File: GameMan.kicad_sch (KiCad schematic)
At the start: 40 parts, among them J1 USB_C_Receptacle_USB2.0_16P, Q1 S8050, SW1 TS-1187A-B-A-B, SW10 TS-1187A-B-A-B, SW11 TS-1187A-B-A-B, SW12 TS-1187A-B-A-B, SW13 TS-1187A-B-A-B, SW2 TS-1187A-B-A-B, SW4 SW_SPST, SW5 TS-1187A-B-A-B, SW6 TS-1187A-B-A-B, SW7 TS-1187A-B-A-B, SW8 TS-1187A-B-A-B, SW9 TS-1187A-B-A-B, U1 ESP32-S3-DEVKITC-1-N8R2, U2 TP4056-42-ESOP8, U3 AMS1117-3.3

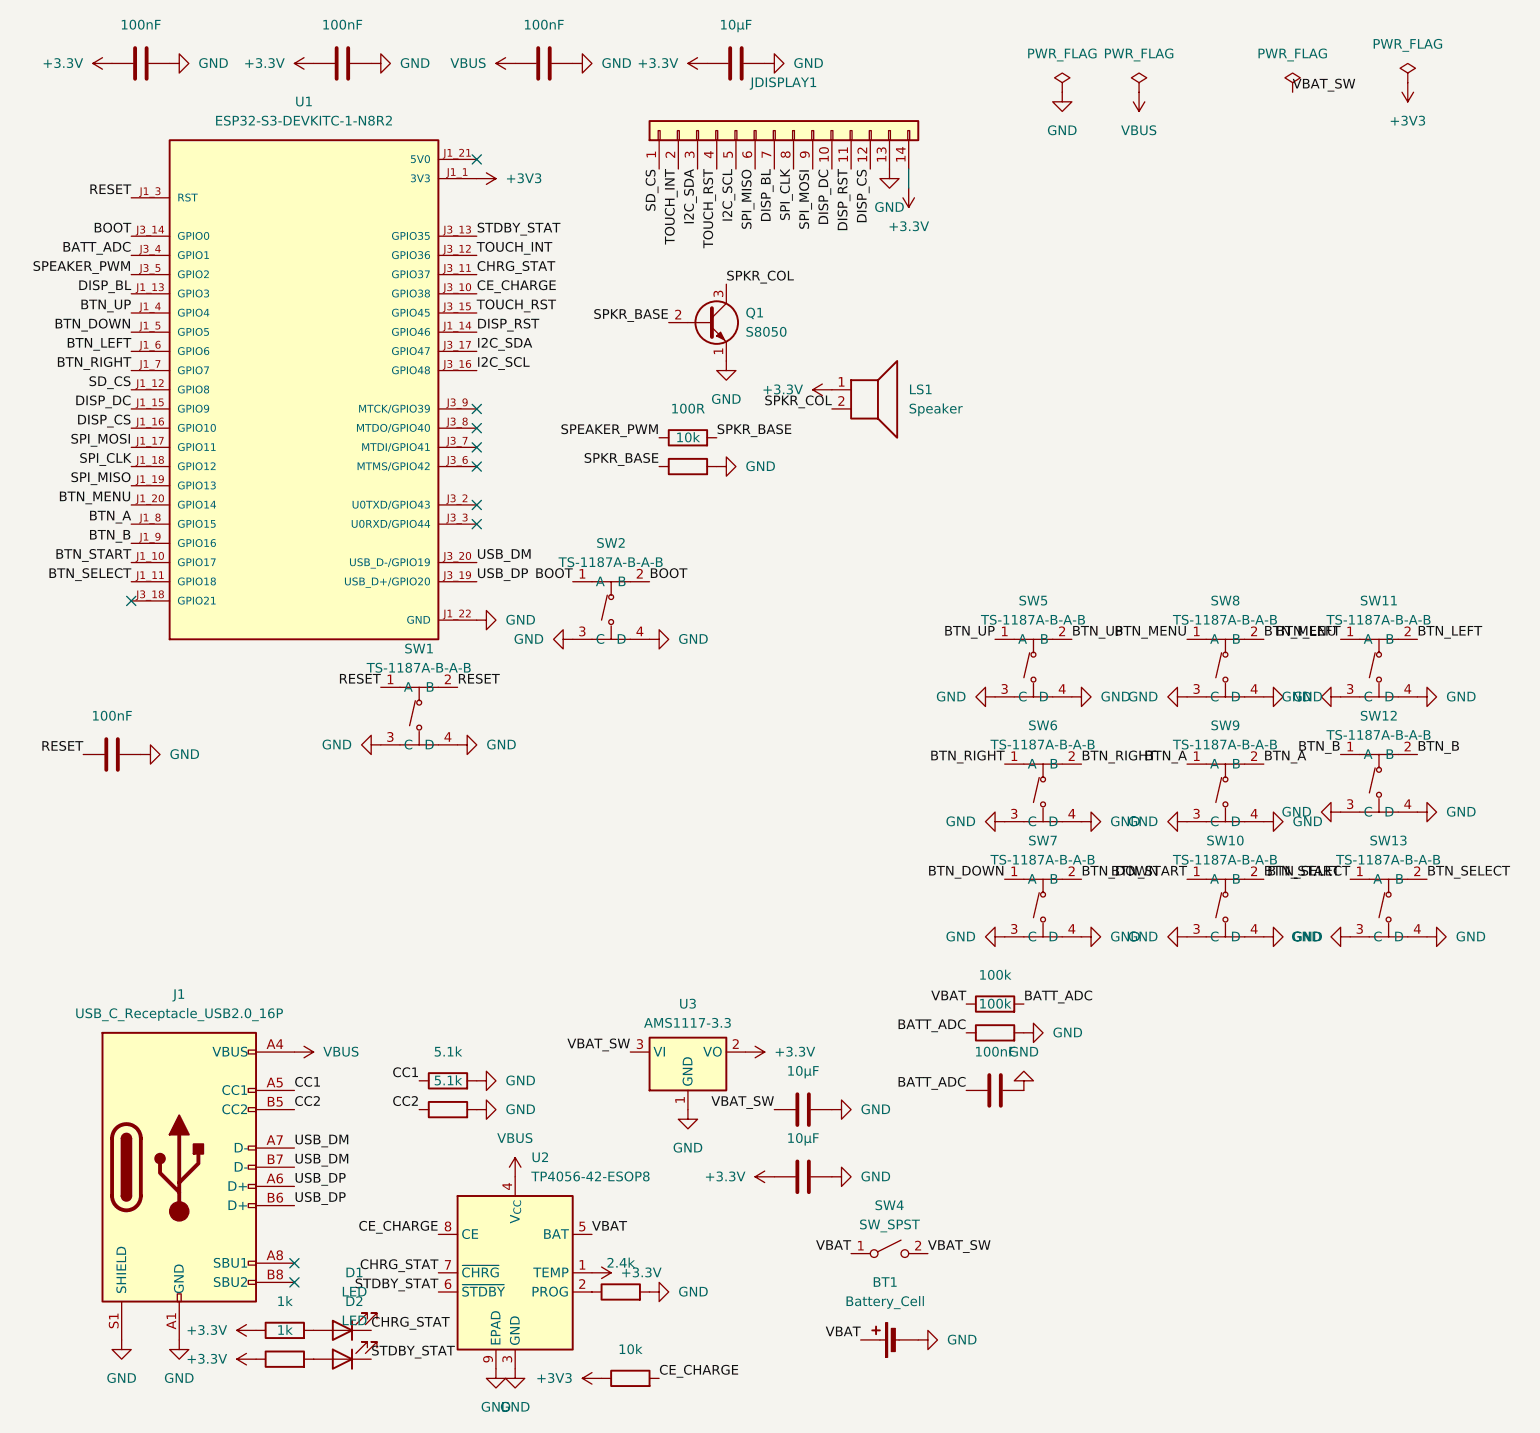
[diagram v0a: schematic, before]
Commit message: PCB layout complete
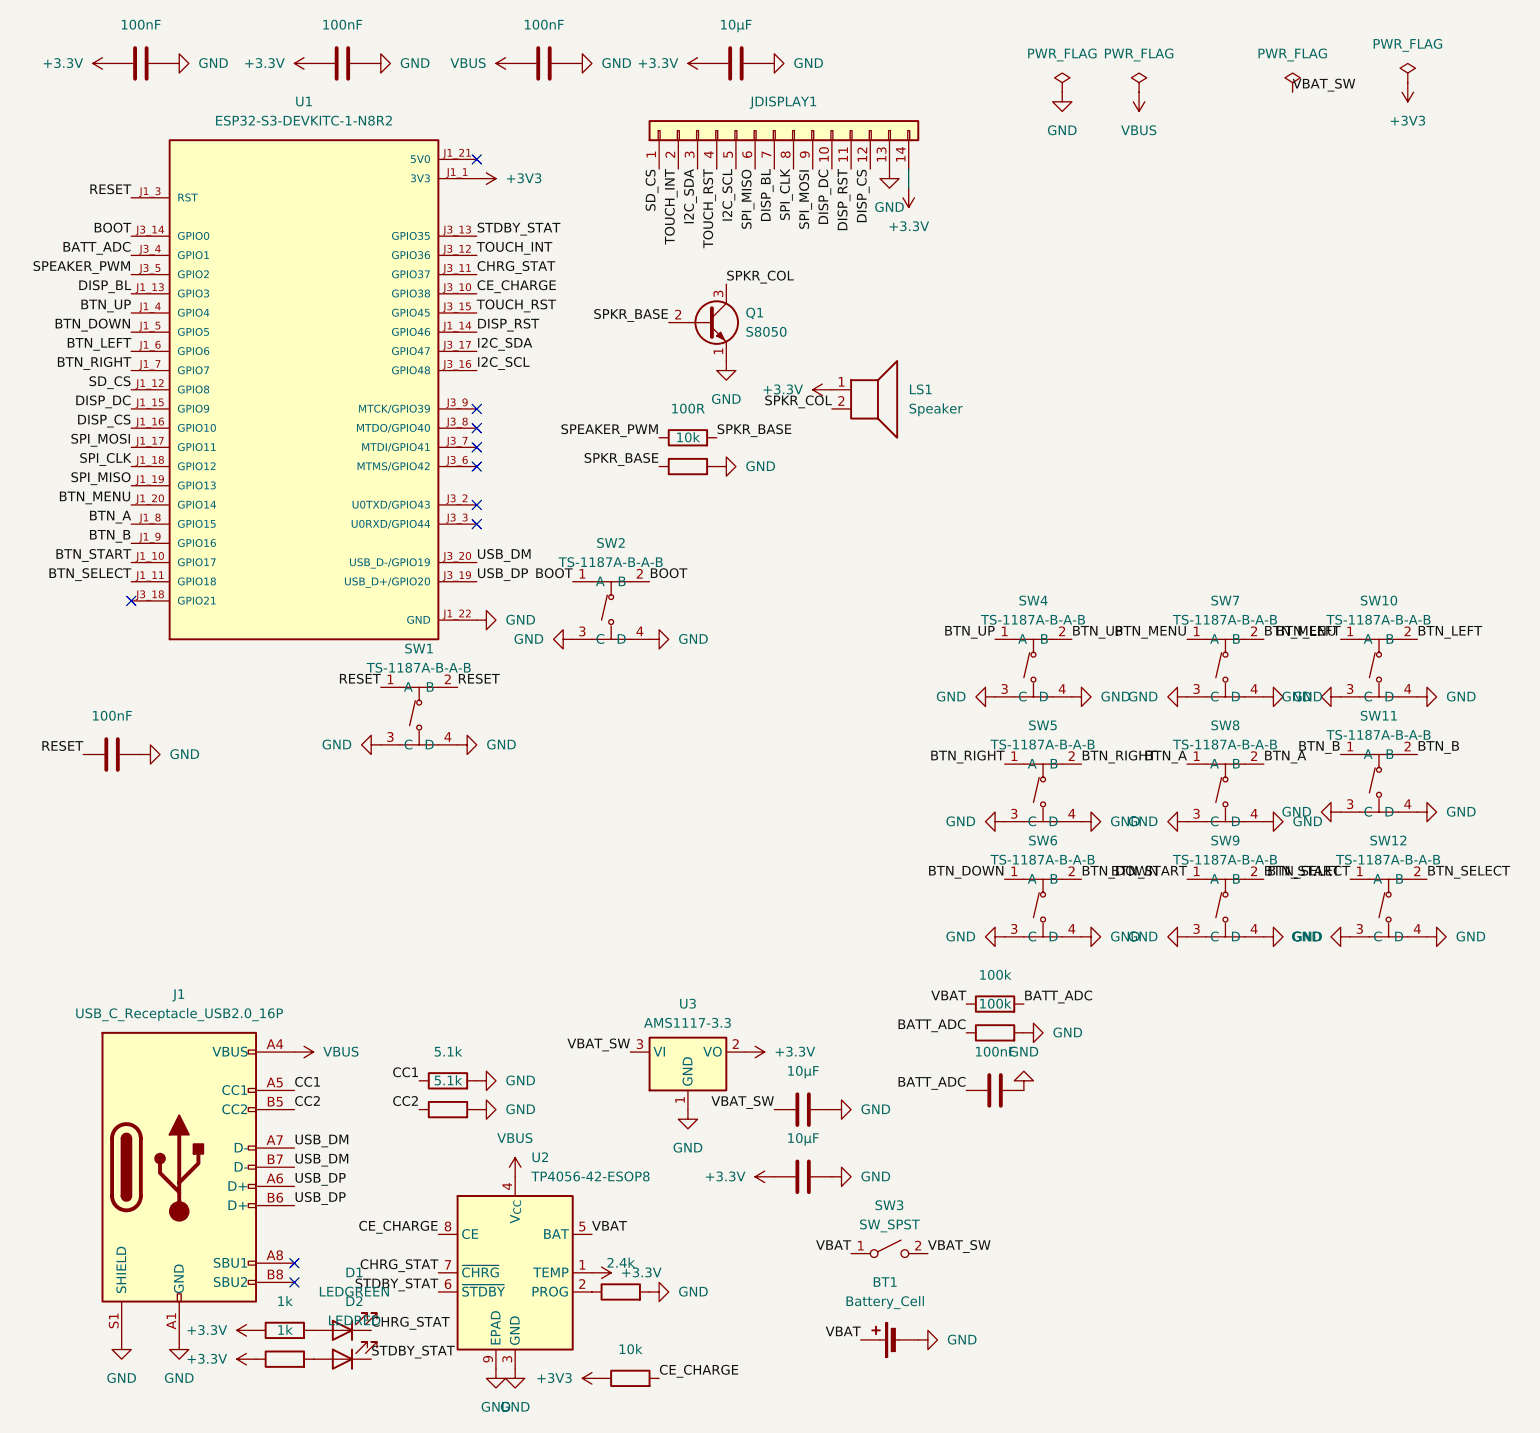
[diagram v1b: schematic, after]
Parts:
- D1: value LED -> LEDGREEN
- D2: value LED -> LEDRED
- J1: footprint (none) -> Connector_USB:USB_C_Receptacle_HRO_TYPE-C-31-M-12
- JDISPLAY1: footprint Connector_PinHeader_1.00mm:PinHeader_1x14_P1.00mm_Vertical -> Connector_PinHeader_2.54mm:PinHeader_1x14_P2.54mm_Vertical
- LS1: footprint (none) -> Connector_PinHeader_2.54mm:PinHeader_1x02_P2.54mm_Vertical
- U1: footprint ESP32-S3-DEVKITC-1-N8R2:XCVR_ESP32-S3-DEVKITC-1-N8R2 -> easyeda:XCVR_ESP32-S3-DEVKITC-1-N8R2
- renumbered SW11 to SW10, SW12 to SW11, SW13 to SW12, SW4 to SW3, SW5 to SW4, SW6 to SW5, SW7 to SW6, SW8 to SW7, SW9 to SW8, SW10 to SW9
